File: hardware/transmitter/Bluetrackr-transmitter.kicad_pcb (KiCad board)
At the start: 2 copper layers, 54 x 30.5 mm, 29 parts, among them J1 Programming_Connector, J2 Battery_Connector, M1 TP4056, M2 MPU-9250, SW1 Button_Reset, SW2 SW_Pair, U1 MIC5205-3.3YM5, U2 STM32F103C8Tx, U3 NRF24L01_Breakout

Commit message: Moved the common libraries to a common folder
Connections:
- net BTN_PAIR renamed /BTN_PAIR
- net LED_POWER renamed /LED_POWER
- net LED_STATUS renamed /LED_STATUS
- net MPU_CS renamed /MPU_CS
- net MPU_INT renamed /MPU_INT
- net NRF_CE renamed /NRF_CE
- net NRF_CS renamed /NRF_CSN
- net NRF_INT renamed /NRF_INT
- net SPI_MISO renamed /SPI_MISO
- net SPI_MOSI renamed /SPI_MOSI
- net SPI_SCK renamed /SPI_SCK
- net SWCLK renamed /SWCLK
- net SWDIO renamed /SWDIO
- net VBAT_SENSE renamed /VBAT_SENSE
- C7 pad 1: Net-(C7-Pad1) -> /NRST
- J1 pad 4: Net-(J1-Pad4) -> /NRST
- R5 pad 2: Net-(C7-Pad1) -> /NRST
- SW1 pad 1: Net-(C7-Pad1) -> /NRST
- U2 pad 7: Net-(C7-Pad1) -> /NRST
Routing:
- net Net-(C7-Pad1): track 29.1 -> 0.00 mm
- net /NRST: track 0.00 -> 29.1 mm

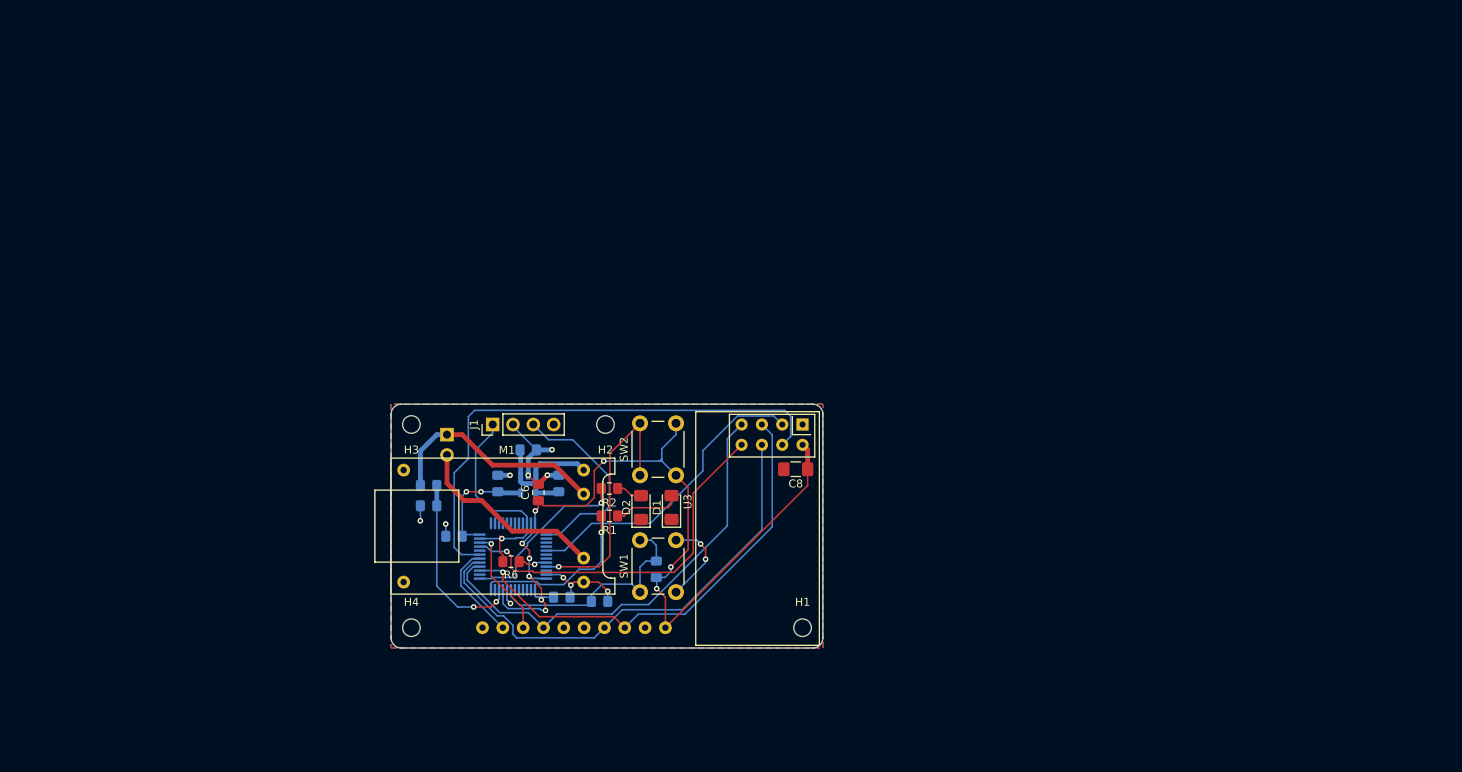
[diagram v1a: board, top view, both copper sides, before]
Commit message: Add board basic dimensions 5x3cm
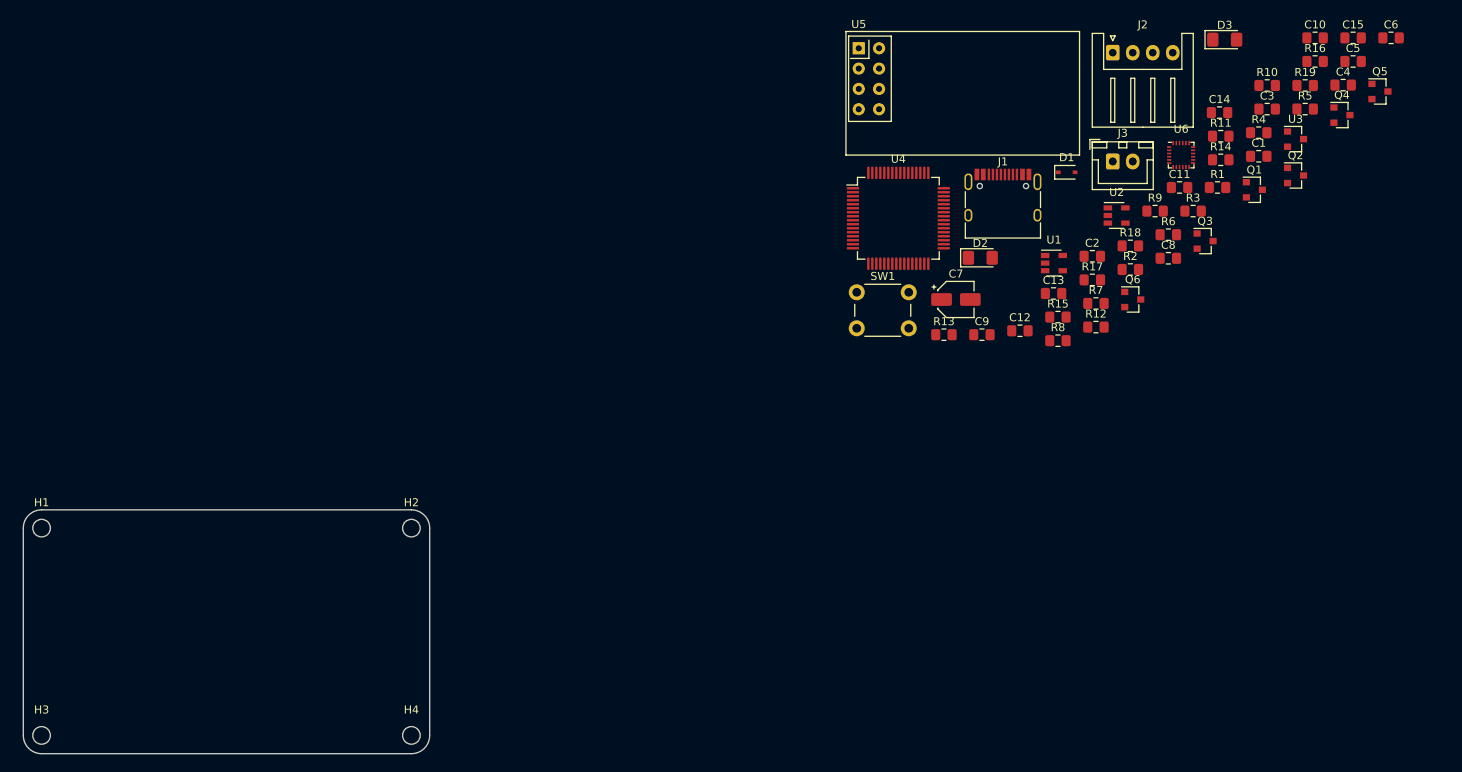
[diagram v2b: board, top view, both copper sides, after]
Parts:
- removed M1: TP4056, Modules:TP4056
- removed M2: MPU-9250, Modules:Module_10pin_15x26mm
- removed SW2: SW_Pair, Button_Switch_THT:SW_PUSH_6mm_H9.5mm
- added C10: 0.1u, Capacitor_SMD:C_0805_2012Metric_Pad1.15x1.40mm_HandSolder, F.Cu at (242.5, 25.3)
- added C11: 0.1u, Capacitor_SMD:C_0805_2012Metric_Pad1.15x1.40mm_HandSolder, F.Cu at (225.6, 44.0)
- added C12: 0.1u, Capacitor_SMD:C_0805_2012Metric_Pad1.15x1.40mm_HandSolder, F.Cu at (205.6, 61.9)
- added C13: 0.1u, Capacitor_SMD:C_0805_2012Metric_Pad1.15x1.40mm_HandSolder, F.Cu at (209.8, 57.3)
- added C14: 0.1u, Capacitor_SMD:C_0805_2012Metric_Pad1.15x1.40mm_HandSolder, F.Cu at (230.6, 34.7)
- added C15: 0.1u, Capacitor_SMD:C_0805_2012Metric_Pad1.15x1.40mm_HandSolder, F.Cu at (247.2, 25.3)
- added C9: 0.1u, Capacitor_SMD:C_0805_2012Metric_Pad1.15x1.40mm_HandSolder, F.Cu at (200.9, 62.4)
- added D3: POWER_LED, LED_SMD:LED_1206_3216Metric_Pad1.42x1.75mm_HandSolder, F.Cu at (231.2, 25.6)
- added J3: Battery_Connector, Connector_JST:JST_XH_B2B-XH-A_1x02_P2.50mm_Vertical, F.Cu at (217.2, 40.8)
- added Q1: CJ2333, Package_TO_SOT_SMD:SOT-23, F.Cu at (234.9, 44.3)
- added Q2: BSS138, Package_TO_SOT_SMD:SOT-23, F.Cu at (240.1, 42.5)
- added Q3: BSS138, Package_TO_SOT_SMD:SOT-23, F.Cu at (228.8, 50.7)
- added Q4: BSS138, Package_TO_SOT_SMD:SOT-23, F.Cu at (245.9, 35.0)
- added Q5: BSS138, Package_TO_SOT_SMD:SOT-23, F.Cu at (250.6, 32.0)
- added Q6: BSS138, Package_TO_SOT_SMD:SOT-23, F.Cu at (219.7, 58.0)
- added R10: 2.2k, Resistor_SMD:R_0805_2012Metric_Pad1.15x1.40mm_HandSolder, F.Cu at (236.5, 31.3)
- added R11: 2.2k, Resistor_SMD:R_0805_2012Metric_Pad1.15x1.40mm_HandSolder, F.Cu at (230.7, 37.6)
- added R12: 2.2k, Resistor_SMD:R_0805_2012Metric_Pad1.15x1.40mm_HandSolder, F.Cu at (215.1, 61.5)
- added R13: 2.2k, Resistor_SMD:R_0805_2012Metric_Pad1.15x1.40mm_HandSolder, F.Cu at (196.1, 62.4)
- added R14: 2.2k, Resistor_SMD:R_0805_2012Metric_Pad1.15x1.40mm_HandSolder, F.Cu at (230.7, 40.6)
- added R15: 2.2k, Resistor_SMD:R_0805_2012Metric_Pad1.15x1.40mm_HandSolder, F.Cu at (210.4, 60.2)
- added R16: 2.2k, Resistor_SMD:R_0805_2012Metric_Pad1.15x1.40mm_HandSolder, F.Cu at (242.5, 28.3)
- added R17: 2.2k, Resistor_SMD:R_0805_2012Metric_Pad1.15x1.40mm_HandSolder, F.Cu at (214.7, 55.6)
- added R18: 2.2k, Resistor_SMD:R_0805_2012Metric_Pad1.15x1.40mm_HandSolder, F.Cu at (219.4, 51.3)
- added R19: 2.2k, Resistor_SMD:R_0805_2012Metric_Pad1.15x1.40mm_HandSolder, F.Cu at (241.3, 31.3)
- added R7: 270, Resistor_SMD:R_0805_2012Metric_Pad1.15x1.40mm_HandSolder, F.Cu at (215.1, 58.5)
- added R8: 470, Resistor_SMD:R_0805_2012Metric_Pad1.15x1.40mm_HandSolder, F.Cu at (210.4, 63.2)
- added R9: 10k, Resistor_SMD:R_0805_2012Metric_Pad1.15x1.40mm_HandSolder, F.Cu at (222.5, 47.0)
- added U4: STM32F030R8Tx, Package_QFP:LQFP-64_10x10mm_P0.5mm, F.Cu at (190.4, 47.9)
- added U5: NRF24L01_Breakout, RF_Module:nRF24L01_Breakout, F.Cu at (185.5, 26.6)
- added U6: ICM-20948, Sensor_Motion:InvenSense_QFN-24_3x3mm_P0.4mm, F.Cu at (225.8, 40.0)
- C1: value 10u -> 1u; moved to F.Cu
- C2: moved to F.Cu
- C3: value 470p -> 10u; moved to F.Cu
- C4: value 100n -> 470p; moved to F.Cu
- C5: value 100n -> 1u; moved to F.Cu
- C6: value 4.7u -> 1u
- C7: value 100n -> 10u; footprint Capacitor_SMD:C_0805_2012Metric_Pad1.15x1.40mm_HandSolder -> Capacitor_SMD:CP_Elec_4x5.4; moved to F.Cu
- C8: value 10u -> 0.1u; footprint Capacitor_SMD:C_1206_3216Metric_Pad1.42x1.75mm_HandSolder -> Capacitor_SMD:C_0805_2012Metric_Pad1.15x1.40mm_HandSolder
- D1: value STATUS_LED -> BAT60J; footprint LED_SMD:LED_1206_3216Metric_Pad1.42x1.75mm_HandSolder -> Diode_SMD:D_SOD-323
- D2: value POWER_LED -> STATUS_LED
- J1: value Programming_Connector -> USB_C_Receptacle_USB2.0; footprint Connector_PinHeader_2.54mm:PinHeader_1x04_P2.54mm_Vertical -> User_Connector_USB:USB_C_Receptacle_HRO_TYPE-C-31-M-12
- J2: value Battery_Connector -> Programming_Connector; footprint Connector_PinHeader_2.54mm:PinHeader_1x02_P2.54mm_Vertical -> Connector_JST:JST_XH_S4B-XH-A_1x04_P2.50mm_Horizontal; moved to F.Cu
- R1: value 2k -> 5.6k
- R2: value 2k -> 47k
- R3: value 47K -> 100k; moved to F.Cu
- R4: value 150k -> 5.1k; moved to F.Cu
- R5: value 10k -> 5.1k; moved to F.Cu
- R6: value 10k -> 100k
- SW1: value Button_Reset -> SW_Pair; footprint Button_Switch_THT:SW_PUSH_6mm_H4.3mm -> Button_Switch_THT:SW_PUSH_6mm_H9.5mm
- U1: value MIC5205-3.3YM5 -> MCP73831-2-OT; moved to F.Cu
- U2: value STM32F103C8Tx -> MIC5205-3.3YM5; footprint Package_QFP:LQFP-48_7x7mm_P0.5mm -> Package_TO_SOT_SMD:SOT-23-5; moved to F.Cu
- U3: value NRF24L01_Breakout -> MCP1700-1802E_SOT23; footprint RF_Module:nRF24L01_Breakout -> Package_TO_SOT_SMD:SOT-23
- moved C5 127.1 mm to (247.2, 28.3), turned to 0 degrees
- moved C6 120.8 mm to (252.0, 25.3), turned to 0 degrees
- moved C4 116.8 mm to (246.0, 31.2)
- moved R4 113.8 mm to (235.5, 37.2)
- moved R3 101.5 mm to (227.2, 47.0), turned to 0 degrees
- moved C3 100.2 mm to (236.5, 34.2), turned to 0 degrees
- moved R5 99.4 mm to (241.3, 34.2), turned to 0 degrees
- moved C1 98.4 mm to (235.5, 40.1)
- moved J2 95.9 mm to (217.2, 27.2), turned to 0 degrees
- moved H1 95.9 mm to (83.3, 86.6)
- moved R6 91.8 mm to (224.2, 49.9), turned to 0 degrees
- moved U2 86.7 mm to (217.7, 47.5), turned to 0 degrees
- moved R1 86.4 mm to (230.3, 44.0)
- moved C2 79.6 mm to (214.7, 52.6), turned to 0 degrees
- moved U1 71.3 mm to (209.9, 53.5), turned to 0 degrees
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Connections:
- C1 pad 1: VDD -> VCC
- C2 pad 1: GND -> VCC
- C2 pad 2: +3V3 -> GND
- C3 pad 1: Net-(C3-Pad1) -> GND
- C3 pad 2: GND -> +3V3
- C4 pad 1: +3V3 -> Net-(C4-Pad1)
- C5 pad 1: +3V3 -> VCC
- C6 pad 1: +3V3 -> +1V8
- C7 pad 1: /NRST -> +3V3
- C8 pad 1: +3V3 -> /NRST
- D1 pad 1: GND -> VCC
- D1 pad 2: Net-(D1-Pad2) -> VBUS
- J2 pad 1: +BATT -> /SWDIO
- J2 pad 2: -BATT -> GND
- R1 pad 1: /LED_STATUS -> Net-(R1-Pad1)
- R1 pad 2: Net-(D1-Pad2) -> GND
- R2 pad 1: /LED_POWER -> /BATT_SENSE
- R2 pad 2: Net-(D2-Pad2) -> +BATT
- R3 pad 1: /VBAT_SENSE -> GND
- R3 pad 2: +BATT -> /BATT_SENSE
- R4 pad 1: GND -> Net-(J1-PadB5)
- R4 pad 2: /VBAT_SENSE -> GND
- R5 pad 1: +3V3 -> Net-(J1-PadA5)
- R5 pad 2: /NRST -> GND
- R6 pad 1: Net-(R6-Pad1) -> GND
- R6 pad 2: GND -> VBUS
- SW1 pad 1: /NRST -> +3V3
- SW1 pad 2: GND -> /BTN_PAIR
- U1 pad 1: VDD -> /CHARGE_STATUS
- U1 pad 3: VDD -> +BATT
- U1 pad 4: Net-(C3-Pad1) -> VBUS
- U1 pad 5: +3V3 -> Net-(R1-Pad1)
- U2 pad 1: +3V3 -> VCC
- U2 pad 2: Net-(U2-Pad2) -> GND
- U2 pad 3: Net-(U2-Pad3) -> VCC
- U2 pad 4: Net-(U2-Pad4) -> Net-(C4-Pad1)
- U2 pad 5: Net-(U2-Pad5) -> +3V3
- U3 pad 2: +3V3 -> +1V8
- U3 pad 3: /NRF_CE -> VCC
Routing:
- net +3V3: track 126.0 -> 0.00 mm, vias 11 -> 0
- net /NRF_CSN: track 65.6 -> 0.00 mm
- net /SPI_MOSI: track 60.8 -> 0.00 mm
- net /SPI_SCK: track 58.7 -> 0.00 mm, vias 1 -> 0
- net /SPI_MISO: track 56.4 -> 0.00 mm
- net GND: track 55.4 -> 0.00 mm, vias 13 -> 0
- net /NRF_INT: track 46.0 -> 0.00 mm, vias 1 -> 0
- net /NRF_CE: track 38.4 -> 0.00 mm
- net /BTN_PAIR: track 33.2 -> 0.00 mm, vias 1 -> 0
- net /NRST: track 29.1 -> 0.00 mm
- net +BATT: track 28.6 -> 0.00 mm
- net /SWCLK: track 25.3 -> 0.00 mm
- net -BATT: track 24.5 -> 0.00 mm
- net /VBAT_SENSE: track 23.0 -> 0.00 mm, vias 2 -> 0
- net /LED_POWER: track 22.6 -> 0.00 mm, vias 1 -> 0
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- removed copper zone on B.Cu, net +3V3
- removed copper zone on F.Cu, net GND
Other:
- board size 54 x 30.5 mm -> 50.8 x 30.5 mm
- rule pad_to_mask_clearance: 0 -> 0.05
- rule trace_min: 0.1524 -> 0.2
- rule via_min_size: 0.508 -> 0.45

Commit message: Began routing the pcb
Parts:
- added C1: 4.7u, Capacitor_SMD:C_0805_2012Metric_Pad1.15x1.40mm_HandSolder, F.Cu at (92.7, 93.1)
- added C3: 4.7u, Capacitor_SMD:C_0805_2012Metric_Pad1.15x1.40mm_HandSolder, F.Cu at (92.7, 86.2)
- C10: renamed from C8; moved to B.Cu
- C15: renamed from C13; moved to B.Cu
- C16: renamed from C14; moved to B.Cu
- C17: renamed from C15; moved to B.Cu
- C7: renamed from C5; moved to B.Cu
- C8: renamed from C6; moved to B.Cu
- C9: renamed from C7; moved to B.Cu
- J2: footprint Connector_JST:JST_XH_S4B-XH-A_1x04_P2.50mm_Horizontal -> Connector_JST:JST_XH_B4B-XH-A_1x04_P2.50mm_Vertical
- J3: footprint Connector_JST:JST_XH_B2B-XH-A_1x02_P2.50mm_Vertical -> Connector_JST:JST_XH_S2B-XH-A_1x02_P2.50mm_Horizontal; moved to B.Cu
- Q2, Q3, Q4, Q5, Q6, R9, U3, U6: moved to B.Cu
- R10, R11, R12, R13, R14, R15, R16, R17, R18, R19: value 2.2k -> 10k; moved to B.Cu
- U2: value MIC5205-3.3YM5 -> MIC5205-2.5YM5
- U5: footprint RF_Module:nRF24L01_Breakout -> Modules:nRF24L01_Breakout
- moved R5 167.9 mm to (83.8, 92.7)
- moved C17 166.6 mm to (102.1, 107.2), turned to 180 degrees
- moved R4 166.5 mm to (84.1, 106.4)
- moved Q5 162.9 mm to (101.4, 97.3), turned to 90 degrees
- moved R16 158.4 mm to (101.4, 100.1), turned to 180 degrees
- moved C8 156.6 mm to (109.0, 89.0), turned to 90 degrees
- moved D3 153.5 mm to (103.4, 110.5)
- moved C12 153.4 mm to (113.8, 108.7)
- moved Q4 153.2 mm to (105.9, 97.3), turned to 90 degrees
- moved C7 152.6 mm to (105.9, 85.9)
- moved C6 150.7 mm to (108.5, 92.7), turned to 180 degrees
- moved C10 147.6 mm to (87.4, 108.5), turned to 90 degrees
- moved R3 147.6 mm to (92.2, 106.4), turned to 90 degrees
- moved J2 147.5 mm to (96.8, 112.3), turned to 180 degrees
- moved C13 145.4 mm to (94.2, 106.4), turned to 90 degrees
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- renumbered C9 to C11, C10 to C12, C11 to C13, C12 to C14, C1 to C2, C2 to C4, C3 to C5, C4 to C6
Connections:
- net +3V3 renamed +2V5
- U4 pad 14: /BATT_SENSE -> Net-(U4-Pad14)
- U4 pad 57: Net-(U4-Pad57) -> /BATT_SENSE
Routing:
- net +2V5: track 0.00 -> 85.0 mm, vias 0 -> 1
- net +1V8: track 0.00 -> 46.6 mm
- net /NRF_CE: track 0.00 -> 26.1 mm
- net /NRF_MISO: track 0.00 -> 25.7 mm
- net /NRF_SCK: track 0.00 -> 24.5 mm
- net VBUS: track 0.00 -> 23.5 mm
- net VCC: track 0.00 -> 22.5 mm, vias 0 -> 1
- net /NRF_CSN: track 0.00 -> 22.3 mm
- net /BTN_PAIR: track 0.00 -> 21.6 mm, vias 0 -> 1
- net /NRF_MOSI: track 0.00 -> 19.7 mm
- net /NRF_INT: track 0.00 -> 18.2 mm
- net +BATT: track 0.00 -> 18.0 mm
- net /LED_STATUS: track 0.00 -> 6.09 mm
- net Net-(R9-Pad1): track 0.00 -> 5.68 mm, vias 0 -> 1
- net /LED_POWER: track 0.00 -> 4.10 mm
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- added copper zone on B.Cu, net GND
- added copper zone on F.Cu, net GND
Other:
- net class Default: clearance 0.2 -> 0.15
- net class Power added: clearance 0.15, trace_width 0.4, via_dia 0.7, via_drill 0.35
- rule trace_clearance: 0.2 -> 0.15

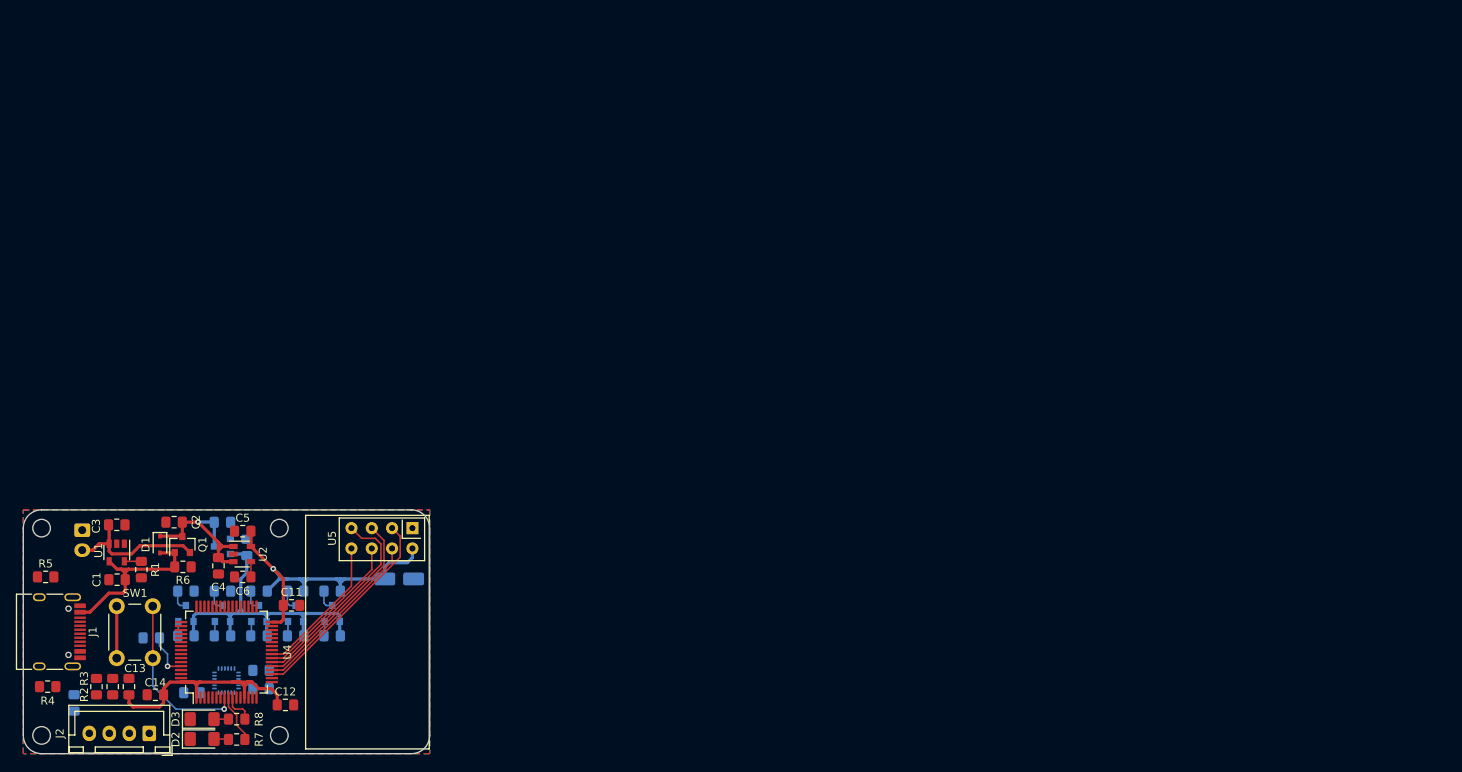
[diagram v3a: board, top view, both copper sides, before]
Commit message: Replace nRF24 breakout with DL-24N nRF24 smd module
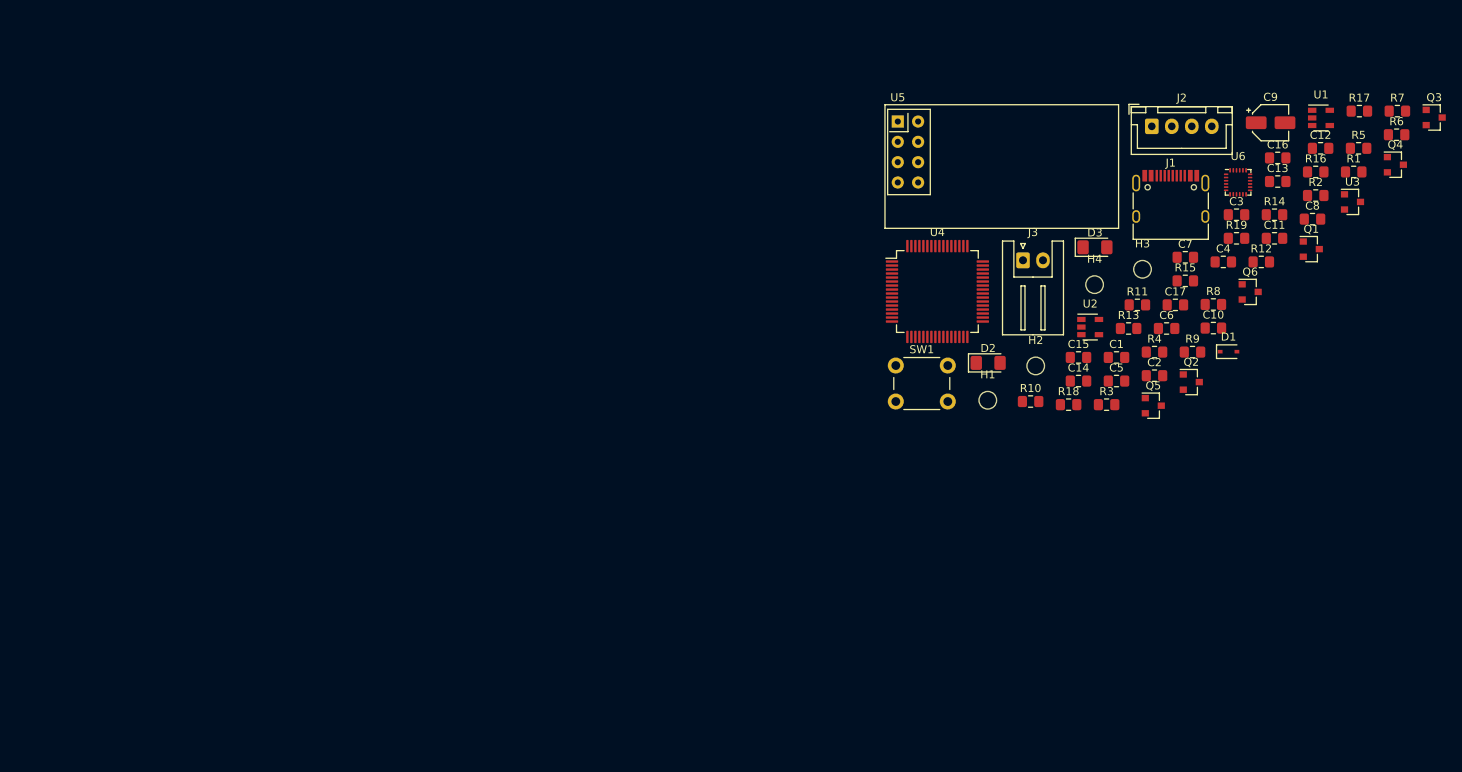
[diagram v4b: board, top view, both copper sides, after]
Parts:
- C10, C15, C16, C17, C7, C8, C9, J3, Q2, Q3, Q4, Q5, Q6, R10, R11, R12, R13, R14, R15, R16, R17, R18, R19, R9, U3, U6: moved to F.Cu
- U5: value NRF24L01_Breakout -> DreamLNK DL-24N-2.4G
- moved R5 172.6 mm to (247.9, 39.1)
- moved R7 165.0 mm to (252.8, 34.5), turned to 0 degrees
- moved R2 164.3 mm to (242.6, 45.0), turned to 0 degrees
- moved R6 161.0 mm to (252.7, 37.4), turned to 0 degrees
- moved U1 160.0 mm to (243.2, 35.3), turned to 0 degrees
- moved R1 159.5 mm to (247.3, 42.1), turned to 0 degrees
- moved Q4 157.0 mm to (252.5, 41.2), turned to 0 degrees
- moved C13 156.9 mm to (237.8, 43.3), turned to 0 degrees
- moved Q3 155.2 mm to (257.4, 35.3), turned to 0 degrees
- moved R16 152.7 mm to (242.6, 42.1), turned to 0 degrees
- moved R17 152.4 mm to (248.0, 34.5), turned to 0 degrees
- moved J1 150.0 mm to (224.5, 46.6), turned to 0 degrees
- moved C10 149.9 mm to (229.8, 61.6), turned to 0 degrees
- moved H3 149.4 mm to (220.9, 54.3)
- moved U3 147.7 mm to (247.2, 45.8), turned to 0 degrees
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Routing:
- net +2V5: track 85.0 -> 0.00 mm, vias 1 -> 0
- net +1V8: track 46.6 -> 0.00 mm
- net /NRF_CE: track 26.1 -> 0.00 mm
- net /NRF_MISO: track 25.7 -> 0.00 mm
- net /NRF_SCK: track 24.5 -> 0.00 mm
- net VBUS: track 23.5 -> 0.00 mm
- net VCC: track 22.5 -> 0.00 mm, vias 1 -> 0
- net /NRF_CSN: track 22.3 -> 0.00 mm
- net /BTN_PAIR: track 21.6 -> 0.00 mm, vias 1 -> 0
- net /NRF_MOSI: track 19.7 -> 0.00 mm
- net /NRF_INT: track 18.2 -> 0.00 mm
- net +BATT: track 18.0 -> 0.00 mm
- net /LED_STATUS: track 6.09 -> 0.00 mm
- net Net-(R9-Pad1): track 5.68 -> 0.00 mm, vias 1 -> 0
- net /LED_POWER: track 4.10 -> 0.00 mm
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- removed copper zone on B.Cu, net GND
- removed copper zone on F.Cu, net GND
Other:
- board outline removed
